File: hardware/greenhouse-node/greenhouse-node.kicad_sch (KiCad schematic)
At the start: 30 parts, among them J1 Conn_01x04_Male, J2 Conn_01x12_Male, J3 Conn_01x02_Male, J4 Conn_01x02_Male, J5 RX_PinHeader_1x04_P2.54mm, J6 TX_PinHeader_1x04_P2.54mm, Q1 BC549C, U1 ATtiny84A-P, U2 L7805, U3 74HC595

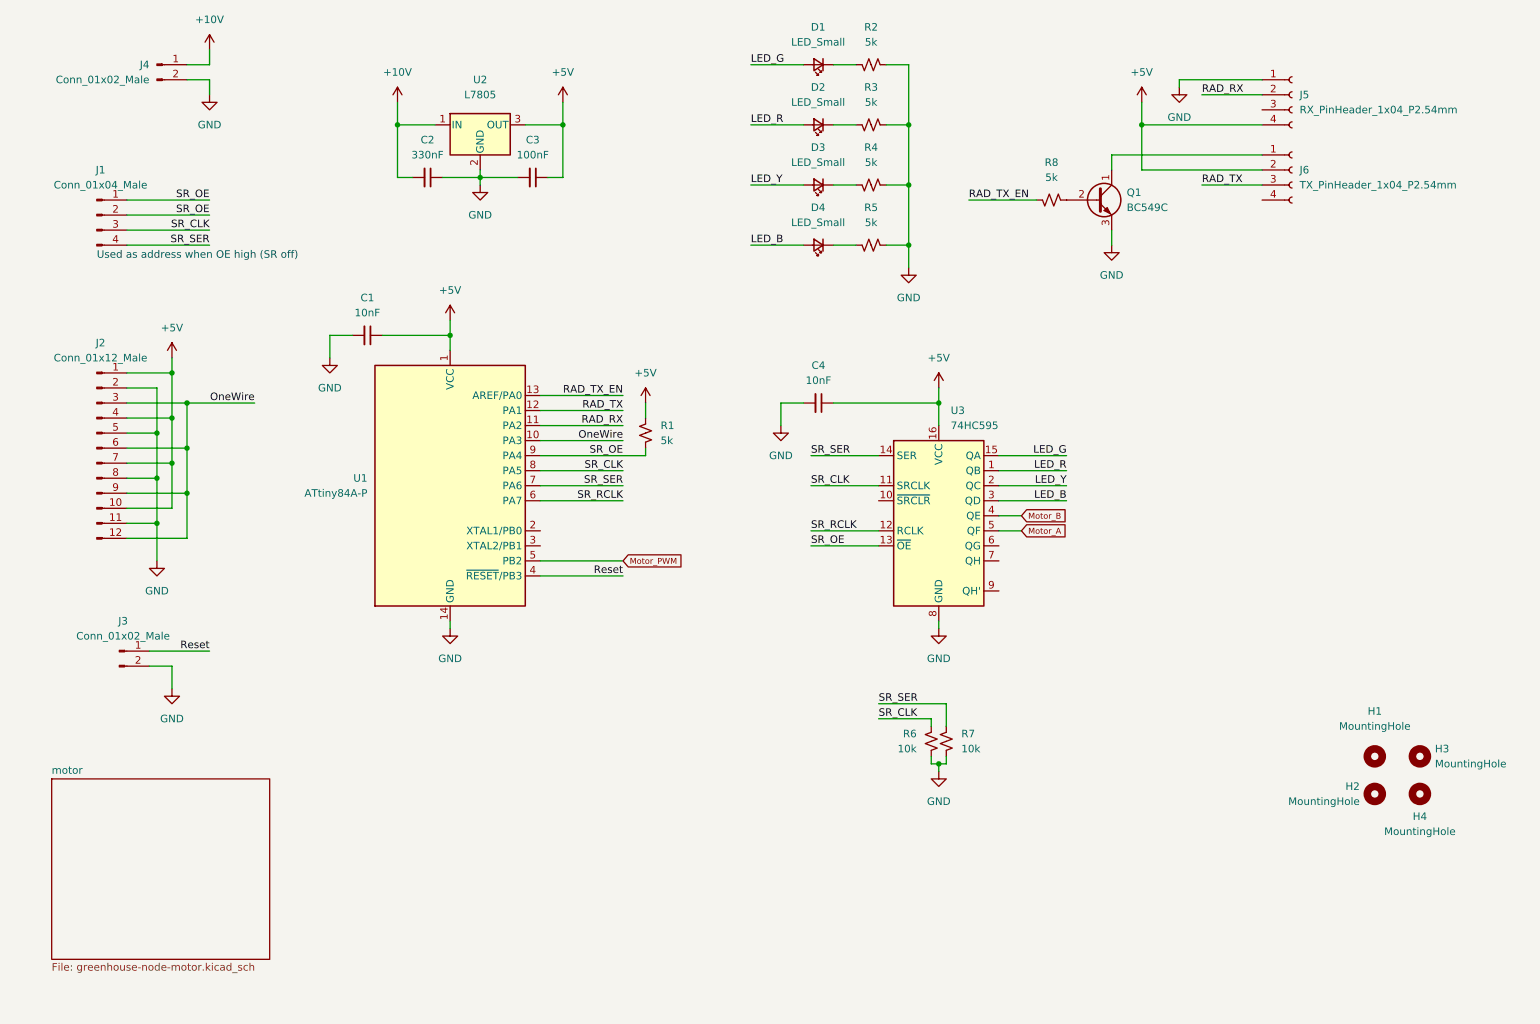
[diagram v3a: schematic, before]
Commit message: Remove address pins
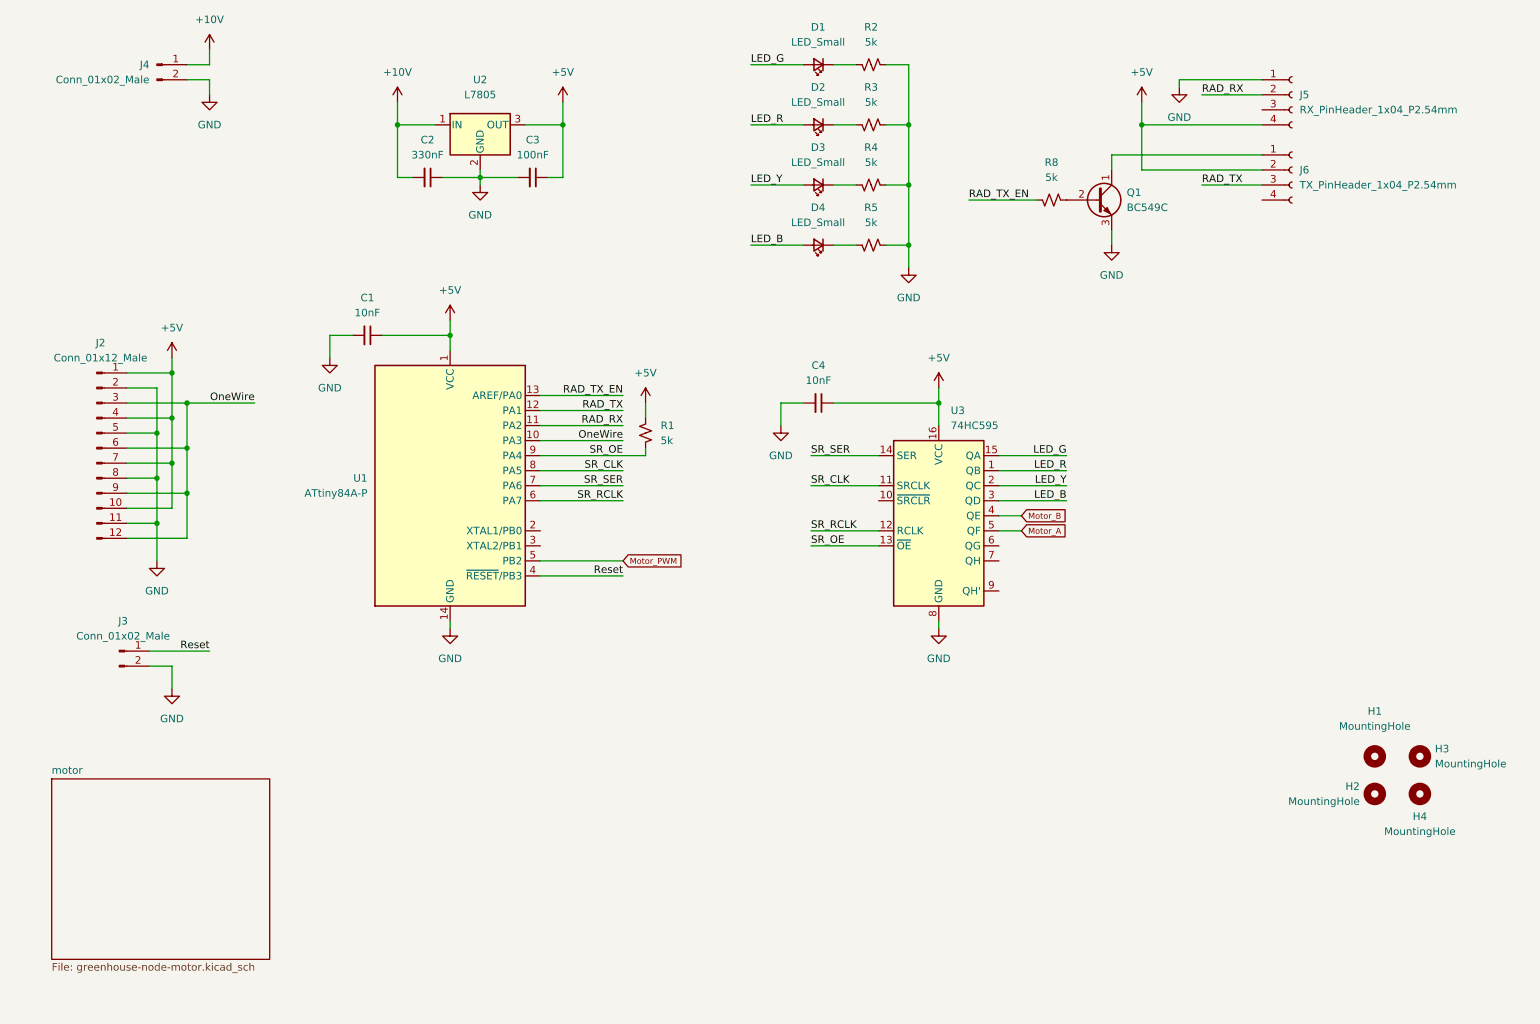
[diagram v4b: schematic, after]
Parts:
- removed J1: Conn_01x04_Male, Connector_PinHeader_2.54mm:PinHeader_2x02_P2.54mm_Vertical, symbol Connector:Conn_01x04_Male
- removed R6, R7: 10k, Resistor_THT:R_Axial_DIN0204_L3.6mm_D1.6mm_P7.62mm_Horizontal, symbol Device:R_Small_US
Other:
- note removed: "Used as address when OE high (SR off)"
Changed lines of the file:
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@@
   (junction (at 106.68 52.07) (diameter 0) (color 0 0 0 0)
   )
-  (junction (at 184.15 151.13) (diameter 0) (color 0 0 0 0)
-  )
   (junction (at 52.07 102.87) (diameter 0) (color 0 0 0 0)
   )
@@
     (stroke (width 0) (type default) (color 0 0 0 0))
   )
-  (wire (pts (xy 185.42 149.86) (xy 185.42 151.13))
-    (stroke (width 0) (type default) (color 0 0 0 0))
-  )
   (wire (pts (xy 116.84 116.84) (xy 130.81 116.84))
     (stroke (width 0) (type default) (color 0 0 0 0))
@@
     (stroke (width 0) (type default) (color 0 0 0 0))
   )
-  (wire (pts (xy 182.88 143.51) (xy 173.99 143.51))
-    (stroke (width 0) (type default) (color 0 0 0 0))
-  )
   (wire (pts (xy 52.07 110.49) (xy 46.99 110.49))
     (stroke (width 0) (type default) (color 0 0 0 0))
@@
     (stroke (width 0) (type default) (color 0 0 0 0))
   )
-  (wire (pts (xy 185.42 151.13) (xy 184.15 151.13))
-    (stroke (width 0) (type default) (color 0 0 0 0))
-  )
-  (wire (pts (xy 182.88 149.86) (xy 182.88 151.13))
-    (stroke (width 0) (type default) (color 0 0 0 0))
-  )
-  (wire (pts (xy 46.99 55.88) (xy 60.96 55.88))
-    (stroke (width 0) (type default) (color 0 0 0 0))
-  )
   (wire (pts (xy 194.31 101.6) (xy 205.74 101.6))
     (stroke (width 0) (type default) (color 0 0 0 0))
   )
-  (wire (pts (xy 184.15 152.4) (xy 184.15 151.13))
-    (stroke (width 0) (type default) (color 0 0 0 0))
-  )
   (wire (pts (xy 60.96 33.02) (xy 57.15 33.02))
     (stroke (width 0) (type default) (color 0 0 0 0))
   )
-  (wire (pts (xy 46.99 63.5) (xy 60.96 63.5))
-    (stroke (width 0) (type default) (color 0 0 0 0))
-  )
   (wire (pts (xy 173.99 104.14) (xy 162.56 104.14))
     (stroke (width 0) (type default) (color 0 0 0 0))
@@
     (stroke (width 0) (type default) (color 0 0 0 0))
   )
-  (wire (pts (xy 173.99 140.97) (xy 185.42 140.97))
-    (stroke (width 0) (type default) (color 0 0 0 0))
-  )
   (wire (pts (xy 54.61 138.43) (xy 54.61 134.62))
     (stroke (width 0) (type default) (color 0 0 0 0))
@@
     (stroke (width 0) (type default) (color 0 0 0 0))
   )
-  (wire (pts (xy 184.15 151.13) (xy 182.88 151.13))
-    (stroke (width 0) (type default) (color 0 0 0 0))
-  )
   (wire (pts (xy 46.99 105.41) (xy 57.15 105.41))
     (stroke (width 0) (type default) (color 0 0 0 0))
@@
     (stroke (width 0) (type default) (color 0 0 0 0))
   )
-  (wire (pts (xy 185.42 140.97) (xy 185.42 144.78))
-    (stroke (width 0) (type default) (color 0 0 0 0))
-  )
   (wire (pts (xy 194.31 99.06) (xy 205.74 99.06))
     (stroke (width 0) (type default) (color 0 0 0 0))
@@
     (stroke (width 0) (type default) (color 0 0 0 0))
   )
-  (wire (pts (xy 182.88 143.51) (xy 182.88 144.78))
-    (stroke (width 0) (type default) (color 0 0 0 0))
-  )
   (wire (pts (xy 213.36 48.26) (xy 238.76 48.26))
     (stroke (width 0) (type default) (color 0 0 0 0))
@@
     (stroke (width 0) (type default) (color 0 0 0 0))
   )
-  (wire (pts (xy 46.99 58.42) (xy 60.96 58.42))
-    (stroke (width 0) (type default) (color 0 0 0 0))
-  )
   (wire (pts (xy 57.15 97.79) (xy 57.15 90.17))
     (stroke (width 0) (type default) (color 0 0 0 0))
@@
     (stroke (width 0) (type default) (color 0 0 0 0))
   )
-  (wire (pts (xy 46.99 60.96) (xy 60.96 60.96))
-    (stroke (width 0) (type default) (color 0 0 0 0))
-  )
   (wire (pts (xy 218.44 50.8) (xy 238.76 50.8))
     (stroke (width 0) (type default) (color 0 0 0 0))
@@
   (wire (pts (xy 152.4 63.5) (xy 161.29 63.5))
     (stroke (width 0) (type default) (color 0 0 0 0))
-  )
-  (text "Used as address when OE high (SR off)" (at 41.91 66.04 0)
-    (effects (font (size 1.27 1.27)) (justify left bottom))
   )
   (label "SR_SER" (at 162.56 99.06 0)
@@
     (effects (font (size 1.27 1.27)) (justify right bottom))
   )
-  (label "SR_OE" (at 60.96 55.88 180)
-    (effects (font (size 1.27 1.27)) (justify right bottom))
-  )
-  (label "SR_CLK" (at 60.96 60.96 180)
-    (effects (font (size 1.27 1.27)) (justify right bottom))
-  )
   (label "OneWire" (at 68.58 90.17 180)
     (effects (font (size 1.27 1.27)) (justify right bottom))
@@
     (effects (font (size 1.27 1.27)) (justify right bottom))
   )
-  (label "SR_OE" (at 60.96 58.42 180)
-    (effects (font (size 1.27 1.27)) (justify right bottom))
-  )
   (label "LED_G" (at 205.74 99.06 180)
     (effects (font (size 1.27 1.27)) (justify right bottom))
@@
     (effects (font (size 1.27 1.27)) (justify left bottom))
   )
-  (label "SR_CLK" (at 173.99 143.51 0)
-    (effects (font (size 1.27 1.27)) (justify left bottom))
-  )
   (label "RAD_TX_EN" (at 189.23 55.88 0)
     (effects (font (size 1.27 1.27)) (justify left bottom))
@@
     (effects (font (size 1.27 1.27)) (justify left bottom))
   )
-  (label "SR_SER" (at 60.96 63.5 180)
-    (effects (font (size 1.27 1.27)) (justify right bottom))
-  )
   (label "LED_Y" (at 205.74 104.14 180)
     (effects (font (size 1.27 1.27)) (justify right bottom))
@@
   (label "Reset" (at 60.96 132.08 180)
     (effects (font (size 1.27 1.27)) (justify right bottom))
-  )
-  (label "SR_SER" (at 173.99 140.97 0)
-    (effects (font (size 1.27 1.27)) (justify left bottom))
   )
   (label "SR_SER" (at 130.81 104.14 180)
@@
     (pin "2")
   )
-  (symbol (lib_id "Device:R_Small_US") (at 185.42 147.32 0) (mirror x) (unit 1)
-    (in_bom yes) (on_board yes) (fields_autoplaced)
-    (property "Reference" "R7" (id 0) (at 187.96 146.0499 0)
-      (effects (font (size 1.27 1.27)) (justify left))
-    )
-    (property "Value" "10k" (id 1) (at 187.96 148.5899 0)
-      (effects (font (size 1.27 1.27)) (justify left))
-    )
-    (property "Footprint" "Resistor_THT:R_Axial_DIN0204_L3.6mm_D1.6mm_P7.62mm_Horizontal" (id 2) (at 185.42 147.32 0)
-      (effects (font (size 1.27 1.27)) hide)
-    )
-    (property "Datasheet" "~" (id 3) (at 185.42 147.32 0)
-      (effects (font (size 1.27 1.27)) hide)
-    )
-    (pin "1")
-    (pin "2")
-  )
   (symbol (lib_id "Device:C_Small") (at 97.79 52.07 270) (unit 1)
     (in_bom yes) (on_board yes) (fields_autoplaced)
@@
     )
     (pin "1")
-  )
-  (symbol (lib_id "Device:R_Small_US") (at 182.88 147.32 0) (mirror x) (unit 1)
-    (in_bom yes) (on_board yes) (fields_autoplaced)
-    (property "Reference" "R6" (id 0) (at 180.4201 146.0499 0)
-      (effects (font (size 1.27 1.27)) (justify right))
-    )
-    (property "Value" "10k" (id 1) (at 180.4201 148.5899 0)
-      (effects (font (size 1.27 1.27)) (justify right))
-    )
-    (property "Footprint" "Resistor_THT:R_Axial_DIN0204_L3.6mm_D1.6mm_P7.62mm_Horizontal" (id 2) (at 182.88 147.32 0)
-      (effects (font (size 1.27 1.27)) hide)
-    )
-    (property "Datasheet" "~" (id 3) (at 182.88 147.32 0)
-      (effects (font (size 1.27 1.27)) hide)
-    )
-    (pin "1")
-    (pin "2")
   )
   (symbol (lib_id "Device:R_Small_US") (at 172.72 43.18 270) (mirror x) (unit 1)
@@
     (pin "1")
   )
-  (symbol (lib_id "Connector:Conn_01x04_Male") (at 41.91 58.42 0) (unit 1)
-    (in_bom yes) (on_board yes) (fields_autoplaced)
-    (property "Reference" "J1" (id 0) (at 42.545 50.8 0))
-    (property "Value" "Conn_01x04_Male" (id 1) (at 42.545 53.34 0))
-    (property "Footprint" "Connector_PinHeader_2.54mm:PinHeader_2x02_P2.54mm_Vertical" (id 2) (at 41.91 58.42 0)
-      (effects (font (size 1.27 1.27)) hide)
-    )
-    (property "Datasheet" "~" (id 3) (at 41.91 58.42 0)
-      (effects (font (size 1.27 1.27)) hide)
-    )
-    (pin "1")
-    (pin "2")
-    (pin "3")
-    (pin "4")
-  )
-  (symbol (lib_id "power:GND") (at 184.15 152.4 0) (unit 1)
-    (in_bom yes) (on_board yes) (fields_autoplaced)
-    (property "Reference" "#PWR017" (id 0) (at 184.15 158.75 0)
-      (effects (font (size 1.27 1.27)) hide)
-    )
-    (property "Value" "GND" (id 1) (at 184.15 157.48 0))
-    (property "Footprint" "" (id 2) (at 184.15 152.4 0)
-      (effects (font (size 1.27 1.27)) hide)
-    )
-    (property "Datasheet" "" (id 3) (at 184.15 152.4 0)
-      (effects (font (size 1.27 1.27)) hide)
-    )
-    (pin "1")
-  )
   (symbol (lib_id "74xx:74HC595") (at 184.15 109.22 0) (unit 1)
     (in_bom yes) (on_board yes) (fields_autoplaced)
@@
       (reference "#PWR016") (unit 1) (value "GND") (footprint "")
     )
-    (path "/e76f0c23-3dcd-483a-a6f9-721673d8aaf1"
-      (reference "#PWR017") (unit 1) (value "GND") (footprint "")
-    )
     (path "/7b7956cd-1bdf-4509-92c9-b55e8439ae86"
       (reference "#PWR018") (unit 1) (value "GND") (footprint "")
@@
       (reference "H4") (unit 1) (value "MountingHole") (footprint "MountingHole:MountingHole_3.2mm_M3")
     )
-    (path "/e3bd1fc9-5e6c-4340-8ab0-e0951ef5bfb4"
-      (reference "J1") (unit 1) (value "Conn_01x04_Male") (footprint "Connector_PinHeader_2.54mm:PinHeader_2x02_P2.54mm_Vertical")
-    )
     (path "/efff4ae7-04da-4400-b348-d5463af9628b"
       (reference "J2") (unit 1) (value "Conn_01x12_Male") (footprint "Connector_Molex:Molex_KK-254_AE-6410-12A_1x12_P2.54mm_Vertical")
@@
       (reference "R5") (unit 1) (value "5k") (footprint "Resistor_THT:R_Axial_DIN0204_L3.6mm_D1.6mm_P7.62mm_Horizontal")
     )
-    (path "/63328a39-50d9-4646-b0c8-2543a598282b"
-      (reference "R6") (unit 1) (value "10k") (footprint "Resistor_THT:R_Axial_DIN0204_L3.6mm_D1.6mm_P7.62mm_Horizontal")
-    )
-    (path "/3d609b48-6700-43fb-ae22-4d2c498a13f3"
-      (reference "R7") (unit 1) (value "10k") (footprint "Resistor_THT:R_Axial_DIN0204_L3.6mm_D1.6mm_P7.62mm_Horizontal")
-    )
     (path "/f8fd57a5-3e5d-466c-801a-1526efadbbc5"

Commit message: Micro programming connector
Also:
- Connect SRCLR to +5V
- Move 10V pull-up away from micro
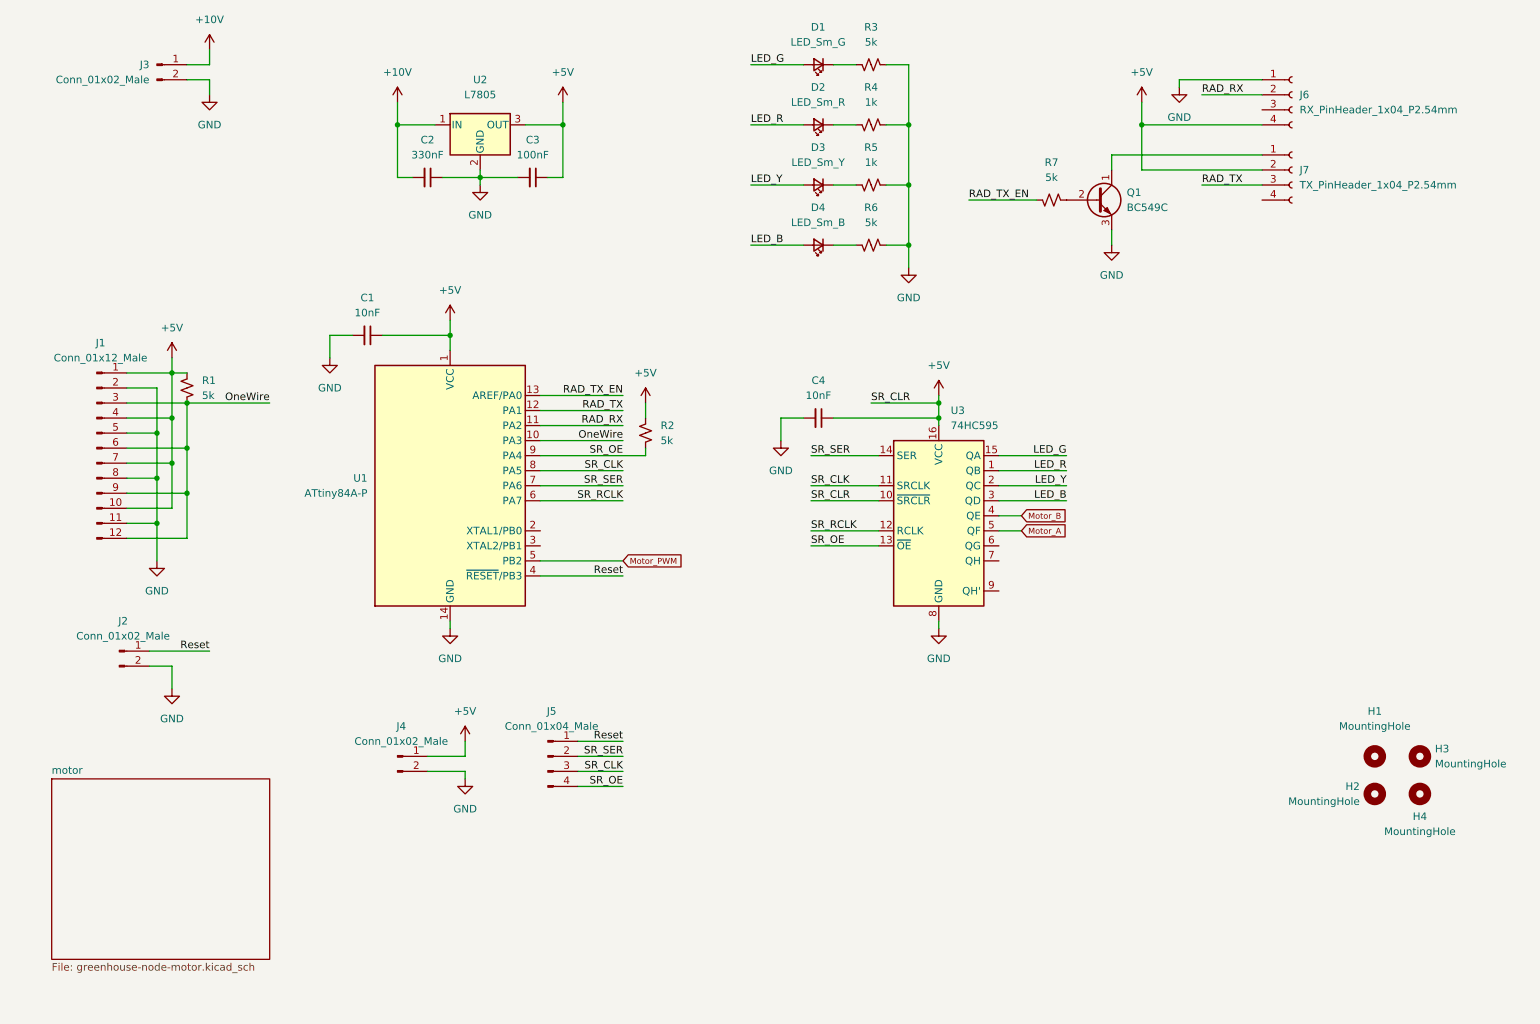
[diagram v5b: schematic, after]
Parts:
- added J4: Conn_01x02_Male, Connector_JST:JST_XH_B2B-XH-A_1x02_P2.50mm_Vertical, symbol Connector:Conn_01x02_Male
- added J5: Conn_01x04_Male, Connector_JST:JST_XH_B4B-XH-A_1x04_P2.50mm_Vertical, symbol Connector:Conn_01x04_Male
- added R1: 5k, Resistor_THT:R_Axial_DIN0204_L3.6mm_D1.6mm_P7.62mm_Horizontal, symbol Device:R_Small_US
- D1: value LED_Small -> LED_Sm_G
- D2: value LED_Small -> LED_Sm_R
- D3: value LED_Small -> LED_Sm_Y
- D4: value LED_Small -> LED_Sm_B
- J2: renamed from J3; footprint Connector_Molex:Molex_KK-254_AE-6410-02A_1x02_P2.54mm_Vertical -> Connector_JST:JST_XH_B2B-XH-A_1x02_P2.50mm_Vertical
- R4: renamed from R3; value 5k -> 1k
- R5: renamed from R4; value 5k -> 1k
- renumbered J2 to J1, J4 to J3, J5 to J6, J6 to J7, R1 to R2, R2 to R3, R5 to R6, R8 to R7
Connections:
- net +5V: now also U3.10 (~{SRCLR}), J4.1 (Pin_1), R1.1
- net GND: now also J4.2 (Pin_2)
- net OneWire: now also R1.2
- net Reset: now also J5.1 (Pin_1)
- net SR_CLK: now also J5.3 (Pin_3)
- net SR_OE: now also J5.4 (Pin_4)
- net SR_SER: now also J5.2 (Pin_2)
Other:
- moved on the sheet: C4
